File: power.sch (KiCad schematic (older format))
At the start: 38 parts, among them J5 Conn_01x02, Q2 AON7405, Q3 Q_NMOS_GSD, U7 MP8759GD, U8 NCP133AMX150TCG

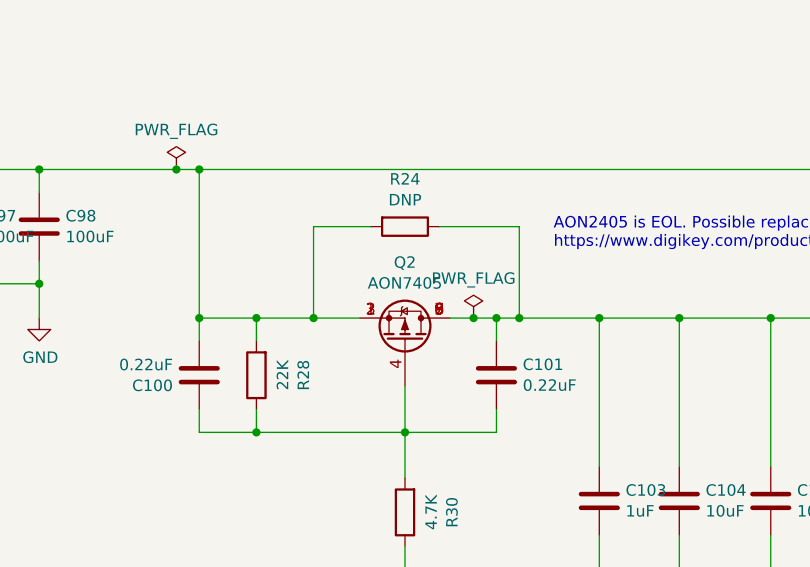
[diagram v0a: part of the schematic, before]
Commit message: Change expansion audio routing to sai2/3
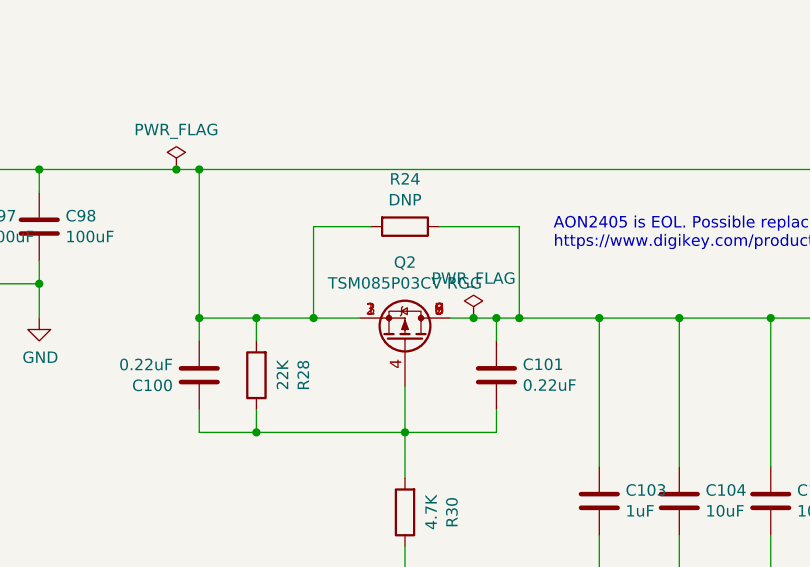
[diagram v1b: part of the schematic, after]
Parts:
- Q2: value AON7405 -> TSM085P03CV RGG; footprint Package_DFN_QFN:DFN-8-1EP_3x3mm_P0.65mm_EP1.7x2.05mm -> Package_DFN_QFN:DFN-8-1EP_3x3mm_P0.65mm_EP1.55x2.4mm; Mfgr AOS -> TSMC; Part AON7405 -> TSM085P03CV RGG; Vendorpart 785-1305-1-ND -> TSM085P03CVRGGCT-ND
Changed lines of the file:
@@
 P 12150 3150
 F 0 "Q2" V 12493 3150 50  0000 C CNN
-F 1 "AON7405" V 12402 3150 50  0000 C CNN
-F 2 "Package_DFN_QFN:DFN-8-1EP_3x3mm_P0.65mm_EP1.7x2.05mm" H 12350 3250 50  0001 C CNN
+F 1 "TSM085P03CV RGG" V 12402 3150 50  0000 C CNN
+F 2 "Package_DFN_QFN:DFN-8-1EP_3x3mm_P0.65mm_EP1.55x2.4mm" H 12350 3250 50  0001 C CNN
 F 3 "~" H 12150 3150 50  0001 C CNN
-F 4 "AOS" H 12150 3150 50  0001 C CNN "Mfgr"
-F 5 "AON7405" H 12150 3150 50  0001 C CNN "Part"
-F 6 "785-1305-1-ND" H 12150 3150 50  0001 C CNN "Vendorpart"
+F 4 "TSMC" H 12150 3150 50  0001 C CNN "Mfgr"
+F 5 "TSM085P03CV RGG" H 12150 3150 50  0001 C CNN "Part"
+F 6 "TSM085P03CVRGGCT-ND" H 12150 3150 50  0001 C CNN "Vendorpart"
 	1    12150 3150
 	0    1    -1   0

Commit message: Fix up main power supply decoupling
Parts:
- removed C97, C98: 100uF, Capacitor_SMD:C_1210_3225Metric, symbol Device:C
- added C91: CP, Capacitor_Tantalum_SMD:CP_EIA-3528-21_Kemet-B, symbol Device:CP
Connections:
- wire segments 143 -> 140
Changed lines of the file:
@@
-	1    0    0    -1
-$EndComp
-$Comp
-L Device:C C97
-U 1 1 5DD07B8D
-P 10200 2650
-F 0 "C97" H 10315 2696 50  0000 L CNN
-F 1 "100uF" H 10315 2605 50  0000 L CNN
-F 2 "Capacitor_SMD:C_1210_3225Metric" H 10238 2500 50  0001 C CNN
-F 3 "~" H 10200 2650 50  0001 C CNN
-F 4 "Murata" H 10200 2650 50  0001 C CNN "Mfgr"
-F 5 "GRM32EC70J107ME15L" H 10200 2650 50  0001 C CNN "Part"
-F 6 "490-10530-1-ND" H 10200 2650 50  0001 C CNN "Vendorpart"
-	1    10200 2650
-	1    0    0    -1
-$EndComp
-$Comp
-L Device:C C98
-U 1 1 5DD07FFA
-P 10550 2650
-F 0 "C98" H 10665 2696 50  0000 L CNN
-F 1 "100uF" H 10665 2605 50  0000 L CNN
-F 2 "Capacitor_SMD:C_1210_3225Metric" H 10588 2500 50  0001 C CNN
-F 3 "~" H 10550 2650 50  0001 C CNN
-F 4 "Murata" H 10550 2650 50  0001 C CNN "Mfgr"
-F 5 "GRM32EC70J107ME15L" H 10550 2650 50  0001 C CNN "Part"
-F 6 "490-10530-1-ND" H 10550 2650 50  0001 C CNN "Vendorpart"
-	1    10550 2650
 	1    0    0    -1
 $EndComp
 Wire Wire Line
 	9000 2400 9500 2400
-Wire Wire Line
-	10550 2400 10550 2500
 Connection ~ 9000 2400
 Wire Wire Line
 	10200 2500 10200 2400
 Connection ~ 10200 2400
-Wire Wire Line
-	10200 2400 10550 2400
 Wire Wire Line
 	9850 2500 9850 2400
@@
 	10550 3050 10550 2900
 Wire Wire Line
-	10550 2900 10200 2900
-Wire Wire Line
 	9500 2900 9500 2800
-Connection ~ 10550 2900
-Wire Wire Line
-	10550 2900 10550 2800
 Wire Wire Line
 	9850 2900 9850 2800
@@
 Wire Wire Line
 	9850 2900 9500 2900
-Wire Wire Line
-	10200 2900 10200 2800
-Connection ~ 10200 2900
-Wire Wire Line
-	10200 2900 9850 2900
-Connection ~ 10550 2400
 Wire Wire Line
 	14150 2400 11250 2400
@@
 	3350 2800 3350 2900
 Wire Wire Line
-	10550 2400 11150 2400
+	9850 2900 10200 2900
+Wire Wire Line
+	10200 2400 11150 2400
+$Comp
+L Device:CP C91
+U 1 1 5E62AAE9
+P 10200 2650
+F 0 "C91" H 10318 2741 50  0000 L CNN
+F 1 "CP" H 10318 2650 50  0000 L CNN
+F 2 "Capacitor_Tantalum_SMD:CP_EIA-3528-21_Kemet-B" H 10238 2500 50  0001 C CNN
+F 3 "~" H 10200 2650 50  0001 C CNN
+F 4 "399-5756-1-ND" H 10318 2559 50  0000 L CNN "Vendorpart"
+F 5 "Kemet" H 10200 2650 50  0001 C CNN "Mfgr"
+F 6 "T520B227M006ATE070" H 10200 2650 50  0001 C CNN "Part"
+	1    10200 2650
+	1    0    0    -1
+$EndComp
+Wire Wire Line
+	10200 2800 10200 2900
+Connection ~ 10200 2900
+Wire Wire Line
+	10200 2900 10550 2900
 $EndSCHEMATC

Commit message: Change power input to JST-PH
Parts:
- C91: symbol Device:CP -> Device:CP1
- J5: footprint Connector_JST:JST_XH_B2B-XH-A_1x02_P2.50mm_Vertical -> Connector_JST:JST_PH_S2B-PH-K_1x02_P2.00mm_Horizontal; Part SM02B-GHS-TB(LF)(SN) -> S2B-PH-K-S(LF)(SN); Vendorpart 455-1564-1-ND -> 455-1719-ND
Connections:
- net labels added: VCHG
- net labels removed: VBUS_IN
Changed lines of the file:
@@
 	0    1    1    0
 $EndComp
-$Comp
-L Device:C C92
-U 1 1 5DC993B7
-P 3350 2650
-F 0 "C92" H 3465 2696 50  0000 L CNN
-F 1 "0.1uF" H 3465 2605 50  0000 L CNN
-F 2 "Capacitor_SMD:C_0402_1005Metric" H 3388 2500 50  0001 C CNN
-F 3 "~" H 3350 2650 50  0001 C CNN
-F 4 "Murata" H 3350 2650 50  0001 C CNN "Mfgr"
-F 5 "GRM155R71E104KE14J" H 3350 2650 50  0001 C CNN "Part"
-F 6 "490-14603-1-ND" H 3350 2650 50  0001 C CNN "Vendorpart"
-	1    3350 2650
-	1    0    0    -1
-$EndComp
-$Comp
-L power:GND #PWR0164
-U 1 1 5DC99486
-P 3350 2900
-F 0 "#PWR0164" H 3350 2650 50  0001 C CNN
-F 1 "GND" H 3355 2727 50  0000 C CNN
-F 2 "" H 3350 2900 50  0001 C CNN
-F 3 "" H 3350 2900 50  0001 C CNN
-	1    3350 2900
-	1    0    0    -1
-$EndComp
-Wire Wire Line
-	3350 2500 3350 2400
-Connection ~ 3350 2400
 Wire Wire Line
 	4200 2550 4200 2400
@@
 Text Label 5750 2950 0    50   ~ 0
 VCC_3V6
-$Comp
-L Connector_Generic:Conn_01x02 J?
-U 1 1 5DC815A7
-P 2900 3500
-AR Path="/5DC815A7" Ref="J?"  Part="1"
-AR Path="/5DC6F4F1/5DC815A7" Ref="J5"  Part="1"
-F 0 "J5" H 2980 3492 50  0000 L CNN
-F 1 "Conn_01x02" H 2980 3401 50  0000 L CNN
-F 2 "Connector_JST:JST_XH_B2B-XH-A_1x02_P2.50mm_Vertical" H 2900 3500 50  0001 C CNN
-F 3 "~" H 2900 3500 50  0001 C CNN
-F 4 "JST" H 2900 3500 50  0001 C CNN "Mfgr"
-F 5 "SM02B-GHS-TB(LF)(SN)" H 2900 3500 50  0001 C CNN "Part"
-F 6 "455-1564-1-ND" H 2900 3500 50  0001 C CNN "Vendorpart"
-	1    2900 3500
-	1    0    0    -1
-$EndComp
-$Comp
-L power:GND #PWR0168
-U 1 1 5DC85F93
-P 2600 3800
-F 0 "#PWR0168" H 2600 3550 50  0001 C CNN
-F 1 "GND" H 2605 3627 50  0000 C CNN
-F 2 "" H 2600 3800 50  0001 C CNN
-F 3 "" H 2600 3800 50  0001 C CNN
-	1    2600 3800
-	1    0    0    -1
-$EndComp
-Wire Wire Line
-	2600 3800 2600 3600
-Wire Wire Line
-	2600 2400 2600 3500
 $Comp
 L power:GND #PWR0169
@@
 	2550 6500 2550 6600
 Connection ~ 2550 6600
-Text HLabel 2400 2400 0    50   Input ~ 0
-VBUS_IN
-Wire Wire Line
-	2400 2400 2600 2400
-Connection ~ 2600 2400
 NoConn ~ 6300 3150
 $Comp
@@
 $EndComp
 Connection ~ 11150 2400
-Wire Wire Line
-	2600 3500 2700 3500
-Wire Wire Line
-	2600 3600 2700 3600
 Text Label 7350 2500 0    50   ~ 0
 SW
@@
 Wire Wire Line
 	4500 2850 6300 2850
-Wire Wire Line
-	3350 2400 4200 2400
 $Comp
 L power:GND #PWR0165
@@
 AON2405 is EOL. Possible replacement\nhttps://www.digikey.com/product-detail/en/0/785-AONR21305CTR-ND
 Wire Wire Line
-	2600 2400 3350 2400
-Wire Wire Line
-	3350 2800 3350 2900
-Wire Wire Line
 	9850 2900 10200 2900
 Wire Wire Line
 	10200 2400 11150 2400
 $Comp
-L Device:CP C91
+L Device:CP1 C91
 U 1 1 5E62AAE9
 P 10200 2650
@@
 Wire Wire Line
 	10200 2900 10550 2900
+Text HLabel 2400 2400 0    50   Input ~ 0
+VCHG
+Connection ~ 2600 2400
+Wire Wire Line
+	2400 2400 2600 2400
+Wire Wire Line
+	2600 3600 2700 3600
+Wire Wire Line
+	2600 3500 2700 3500
+Wire Wire Line
+	2600 2400 2600 3500
+Wire Wire Line
+	2600 3800 2600 3600
+$Comp
+L power:GND #PWR0168
+U 1 1 5DC85F93
+P 2600 3800
+F 0 "#PWR0168" H 2600 3550 50  0001 C CNN
+F 1 "GND" H 2605 3627 50  0000 C CNN
+F 2 "" H 2600 3800 50  0001 C CNN
+F 3 "" H 2600 3800 50  0001 C CNN
+	1    2600 3800
+	1    0    0    -1
+$EndComp
+$Comp
+L Connector_Generic:Conn_01x02 J?
+U 1 1 5DC815A7
+P 2900 3500
+AR Path="/5DC815A7" Ref="J?"  Part="1"
+AR Path="/5DC6F4F1/5DC815A7" Ref="J5"  Part="1"
+F 0 "J5" H 2980 3492 50  0000 L CNN
+F 1 "Conn_01x02" H 2980 3401 50  0000 L CNN
+F 2 "Connector_JST:JST_PH_S2B-PH-K_1x02_P2.00mm_Horizontal" H 2900 3500 50  0001 C CNN
+F 3 "~" H 2900 3500 50  0001 C CNN
+F 4 "JST" H 2900 3500 50  0001 C CNN "Mfgr"
+F 5 "S2B-PH-K-S(LF)(SN)" H 2900 3500 50  0001 C CNN "Part"
+F 6 "455-1719-ND" H 2900 3500 50  0001 C CNN "Vendorpart"
+	1    2900 3500
+	1    0    0    -1
+$EndComp
+$Comp
+L power:GND #PWR0164
+U 1 1 5DC99486
+P 3350 2900
+F 0 "#PWR0164" H 3350 2650 50  0001 C CNN
+F 1 "GND" H 3355 2727 50  0000 C CNN
+F 2 "" H 3350 2900 50  0001 C CNN
+F 3 "" H 3350 2900 50  0001 C CNN
+	1    3350 2900
+	1    0    0    -1
+$EndComp
+Wire Wire Line
+	2600 2400 3350 2400
+Wire Wire Line
+	3350 2400 4200 2400
+Connection ~ 3350 2400
+Wire Wire Line
+	3350 2800 3350 2900
+Wire Wire Line
+	3350 2500 3350 2400
+$Comp
+L Device:C C92
+U 1 1 5DC993B7
+P 3350 2650
+F 0 "C92" H 3465 2696 50  0000 L CNN
+F 1 "0.1uF" H 3465 2605 50  0000 L CNN
+F 2 "Capacitor_SMD:C_0402_1005Metric" H 3388 2500 50  0001 C CNN
+F 3 "~" H 3350 2650 50  0001 C CNN
+F 4 "Murata" H 3350 2650 50  0001 C CNN "Mfgr"
+F 5 "GRM155R71E104KE14J" H 3350 2650 50  0001 C CNN "Part"
+F 6 "490-14603-1-ND" H 3350 2650 50  0001 C CNN "Vendorpart"
+	1    3350 2650
+	1    0    0    -1
+$EndComp
 $EndSCHEMATC

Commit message: Switch 5V buck for 1S battery charger boost
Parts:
- removed C91: CP, Capacitor_Tantalum_SMD:CP_EIA-3528-21_Kemet-B, symbol Device:CP1
- removed D2: D_Zener, Diode_SMD:D_SOD-323, symbol Device:D_Zener
- removed U7: MP8759GD, mxenc:QFN-16_2x3_Pitch0.5mm, symbol mxenc:MP8759GD
- added C162, C163: 22uF, Capacitor_SMD:C_0603_1608Metric, symbol Device:C
- added C173: 0.1uF, Capacitor_SMD:C_0402_1005Metric, symbol Device:C
- added C97, C98: 1uF, Capacitor_SMD:C_0402_1005Metric, symbol Device:C
- added D2, D7, D8: LED, LED_SMD:LED_0603_1608Metric, symbol Device:LED
- added R50: 5.1K, Resistor_SMD:R_0201_0603Metric, symbol Device:R
- added R51: 20m, Resistor_SMD:R_1206_3216Metric, symbol Device:R
- added R53: 13.3K, Resistor_SMD:R_0201_0603Metric, symbol Device:R
- added R60, R61, R62, R63, R64: 10K, Resistor_SMD:R_0201_0603Metric, symbol Device:R
- added R65, R66, R67: 680, Resistor_SMD:R_0201_0603Metric, symbol Device:R
- added U7: MP2636GR-P, mxenc:IC_MP2636GR-P, symbol mxenc:MP2636GR-P
- C102: value 1uF -> 22uF; footprint Capacitor_SMD:C_0402_1005Metric -> Capacitor_SMD:C_0603_1608Metric; Part GRM155C81A105KA12D -> GRM188C80G226MEA0D; Vendorpart 490-12699-1-ND -> 490-7196-1-ND
- C104: footprint Capacitor_SMD:C_0805_2012Metric_Pad1.15x1.40mm_HandSolder -> Capacitor_SMD:C_0805_2012Metric
- C94: value 0.22uF -> 1uF; Part GRM155C8YA224ME01D -> GRM155C81A105KA12D; Vendorpart 490-10446-1-ND -> 490-12699-1-ND
- C95: value 0.1uF -> 1uF; Part GRM155R71E104KE14J -> GRM155C81A105KA12D; Vendorpart 490-14603-1-ND -> 490-12699-1-ND
- C96: value 100uF -> DNP; footprint Capacitor_SMD:C_1210_3225Metric -> Capacitor_SMD:C_0402_1005Metric; Mfgr Murata -> (none); Part GRM32EC70J107ME15L -> (none); Vendorpart 490-10530-1-ND -> (none)
- C99: value DNP -> 22uF; footprint Capacitor_SMD:C_0402_1005Metric -> Capacitor_SMD:C_0603_1608Metric; Mfgr (none) -> Murata; Part (none) -> GRM188C80G226MEA0D; Vendorpart (none) -> 490-7196-1-ND
- R19: value DNP -> 15K; footprint Resistor_SMD:R_0402_1005Metric -> Resistor_SMD:R_0201_0603Metric; Mfgr (none) -> Yageo; Part (none) -> RC0201FR-0715KL; Vendorpart (none) -> YAG2423CT-ND
- R20: value 100K -> 23.7K; footprint Resistor_SMD:R_0402_1005Metric -> Resistor_SMD:R_0201_0603Metric; Part RC0402JR-07100KL -> RC0201FR-0723K7L; Vendorpart 311-100KJRCT-ND -> YAG2524CT-ND
- R21: value 3.3 -> 39K; footprint Resistor_SMD:R_0603_1608Metric -> Resistor_SMD:R_0201_0603Metric; Mfgr Vishay Beyschlag -> Yageo; Part MCT06030C3308FP500 -> RC0201FR-0739KL; Vendorpart 749-1639-1-ND -> YAG2641CT-ND
- R22: value 100K -> 120K; footprint Resistor_SMD:R_0402_1005Metric -> Resistor_SMD:R_0201_0603Metric; Part RC0402JR-07100KL -> AC0201FR-07120KL; Vendorpart 311-100KJRCT-ND -> YAG5150CT-ND
- R25: value 499K DNP -> 10K; footprint Resistor_SMD:R_0402_1005Metric -> Resistor_SMD:R_0201_0603Metric; Mfgr (none) -> Yageo; Part (none) -> RC0201FR-0710KL; Vendorpart (none) -> 311-10.0KMCT-ND
- R26: value 41.2K -> 31.6K; footprint Resistor_SMD:R_0402_1005Metric -> Resistor_SMD:R_0201_0603Metric; Mfgr Panasonic -> Yageo; Part ERJ-2RKF4122X -> RC0201FR-0731K6L; Vendorpart P41.2KLCT-ND -> YAG2597CT-ND
- R27: value DNP -> 5.1K; footprint Resistor_SMD:R_0402_1005Metric -> Resistor_SMD:R_0201_0603Metric; Mfgr (none) -> Yageo; Part (none) -> RC0201FR-075K1L; Vendorpart (none) -> YAG2741CT-ND
- R29: value 5.6K -> 10K; footprint Resistor_SMD:R_0402_1005Metric -> Resistor_SMD:R_0201_0603Metric; Mfgr Panasonic -> Yageo; Part ERJ-2RKF5601X -> RC0201FR-0710KL; Vendorpart P5.60KLCT-ND -> 311-10.0KMCT-ND
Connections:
- net labels added: CHG_EN, CSP, FB_DIV, FREQ, GNDA, IB, ILIM, ISET, NTC, OLIM, PWIN, REG, TMR, VB, VBATT, VCC, VIB, ~ACOK, ~BOOST, ~CHG
- net labels removed: BST, VCC_3V6
- wire segments 140 -> 181
- no-connect marks 1 -> 0
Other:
- note added: "1A charge\ncurrent"
- note added: "3.2A input\ncurrent"
- note added: "5V 3A"
- note added: "Iolim(A) = 2400 / (Rolim (k) * RS1 (m))\nRS1 = 20m\nIolim = 3.0A"
- note removed: "5V/8A"
- note removed: "EN internal pulldown 600K"
- moved on the sheet: C92, J5, L7, R18, R22, R26

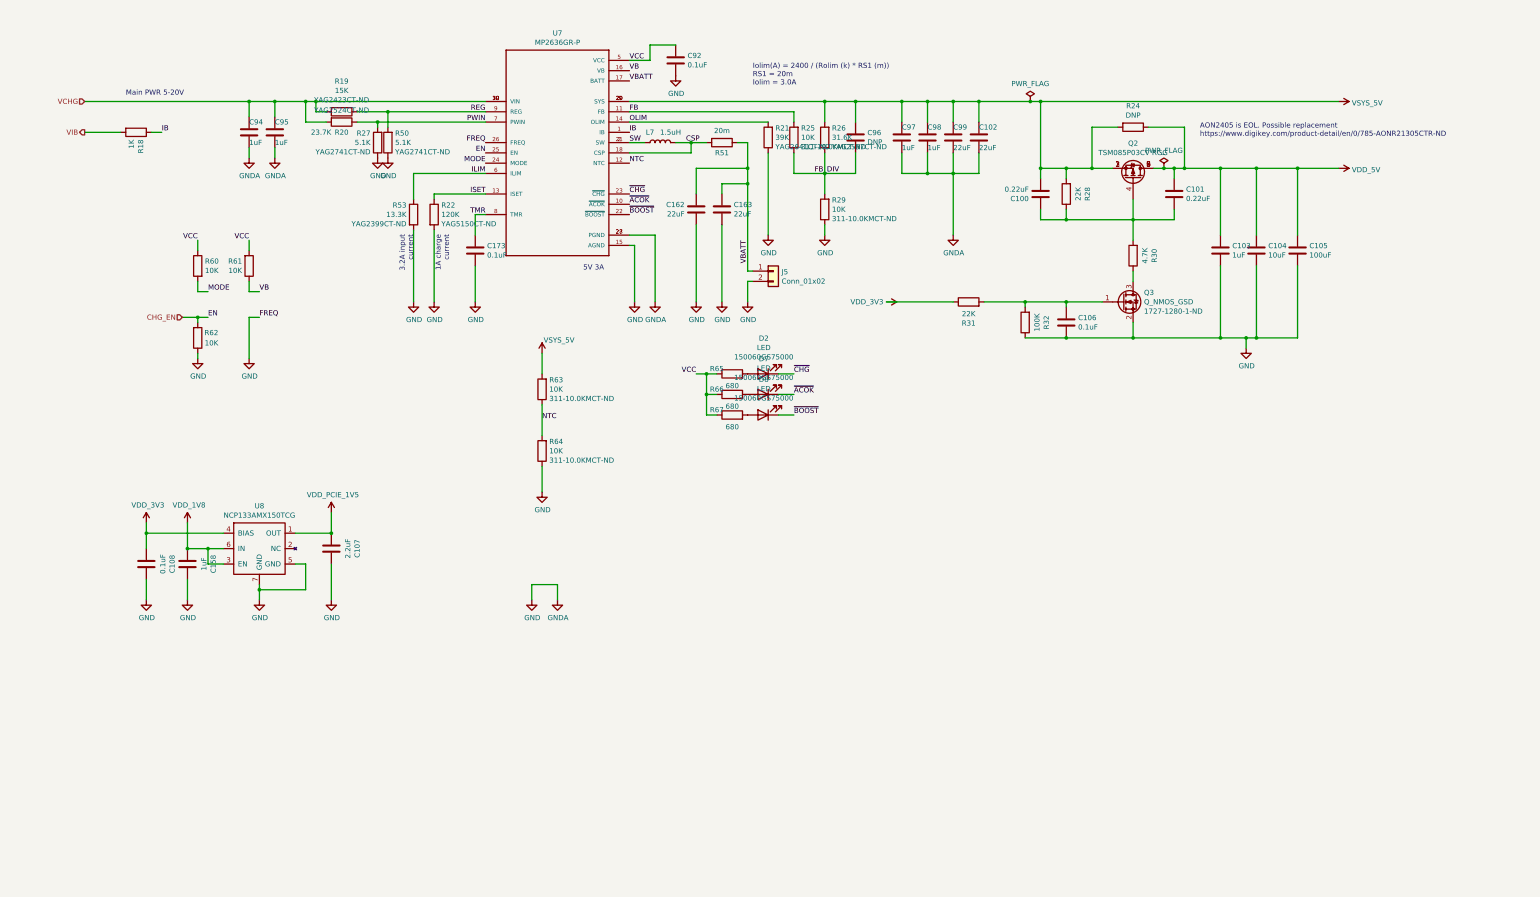
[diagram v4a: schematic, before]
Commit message: Added PicoSPOX battery connection option w/ NTC
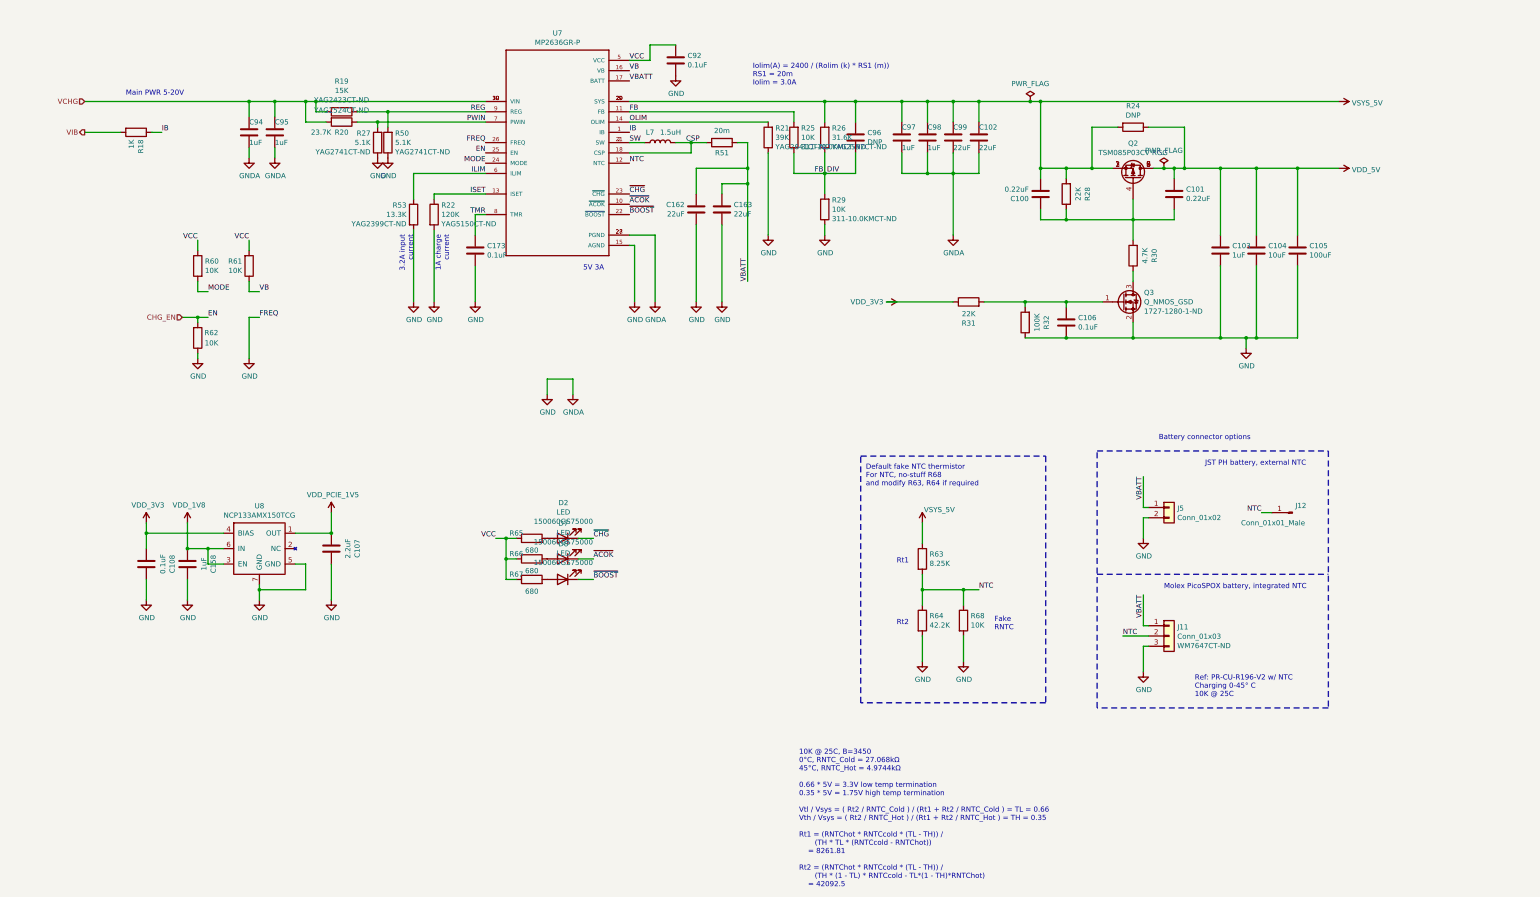
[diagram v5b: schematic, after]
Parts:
- added J11: Conn_01x03, mxenc:PicoSPOX_SMD_RA_3POS, symbol Connector_Generic:Conn_01x03
- added J12: Conn_01x01_Male, TestPoint:TestPoint_THTPad_D1.5mm_Drill0.7mm, symbol Connector:Conn_01x01_Male
- added R68: 10K, Resistor_SMD:R_0402_1005Metric, symbol Device:R
- R63: value 10K -> 8.25K; footprint Resistor_SMD:R_0201_0603Metric -> Resistor_SMD:R_0402_1005Metric; Part RC0201FR-0710KL -> RC0402FR-078K25L; Vendorpart 311-10.0KMCT-ND -> 311-8.25KLRCT-ND
- R64: value 10K -> 42.2K; footprint Resistor_SMD:R_0201_0603Metric -> Resistor_SMD:R_0402_1005Metric; Part RC0201FR-0710KL -> RC0402FR-0742K2L; Vendorpart 311-10.0KMCT-ND -> 311-42.2KLRCT-ND
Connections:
- net GND: now also R64.2, J11.3 (Pin_3), R68.2; no longer R64.1
- net NTC: now also R63.2, R64.1, J11.2 (Pin_2), J12.1 (Pin_1), R68.1; no longer R63.1, R64.2
- net VBATT: now also J11.1 (Pin_1)
- net VSYS_5V: now also R63.1; no longer R63.2
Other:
- note added: "10K @ 25C, B=3450\n0°C, RNTC_Cold = 27.068kΩ\n45°C, RNTC_Hot = 4.9744kΩ\n\n0.66 * 5V = 3.3V low temp termination\n0.35 * 5V = 1.75V high temp termination\n\nVtl / Vsys = ( Rt2 / RNTC_Cold ) / (Rt1 + Rt2 / RNTC_Cold ) = TL = 0.66\nVth / Vsys = ( Rt2 / RNTC_Hot ) / (Rt1 + Rt2 / RNTC_Hot ) = TH = 0.35\n\nRt1 = (RNTChot * RNTCcold * (TL - TH)) /\n (TH * TL * (RNTCcold - RNTChot))\n = 8261.81\n\nRt2 =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"
- note added: "Battery connector options"
- note added: "Default fake NTC thermistor\nFor NTC, no-stuff R68\nand modify R63, R64 if required"
- note added: "Fake\nRNTC"
- note added: "JST PH battery, external NTC"
- note added: "Molex PicoSPOX battery, integrated NTC"
- note added: "Ref: PR-CU-R196-V2 w/ NTC\nCharging 0-45° C\n10K @ 25C"
- note added: "Rt1"
- note added: "Rt2"
- note removed: "AON2405 is EOL. Possible replacement\nhttps://www.digikey.com/product-detail/en/0/785-AONR21305CTR-ND"
- moved on the sheet: D2, D7, D8, J5, R65, R66, R67
